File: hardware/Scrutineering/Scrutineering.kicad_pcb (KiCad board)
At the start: 2 copper layers, 52.8 x 51.7 mm, 22 parts, among them J1 Conn_02x04, J10 Conn_01x01, J11 Conn_01x02, J12 Conn_01x02, J2 Conn_02x04, J3 Conn_01x03, J4 Conn_01x03, J5 Conn_01x01, J6 Conn_01x01, J7 Conn_01x01, J8 Conn_01x01, J9 Conn_01x01

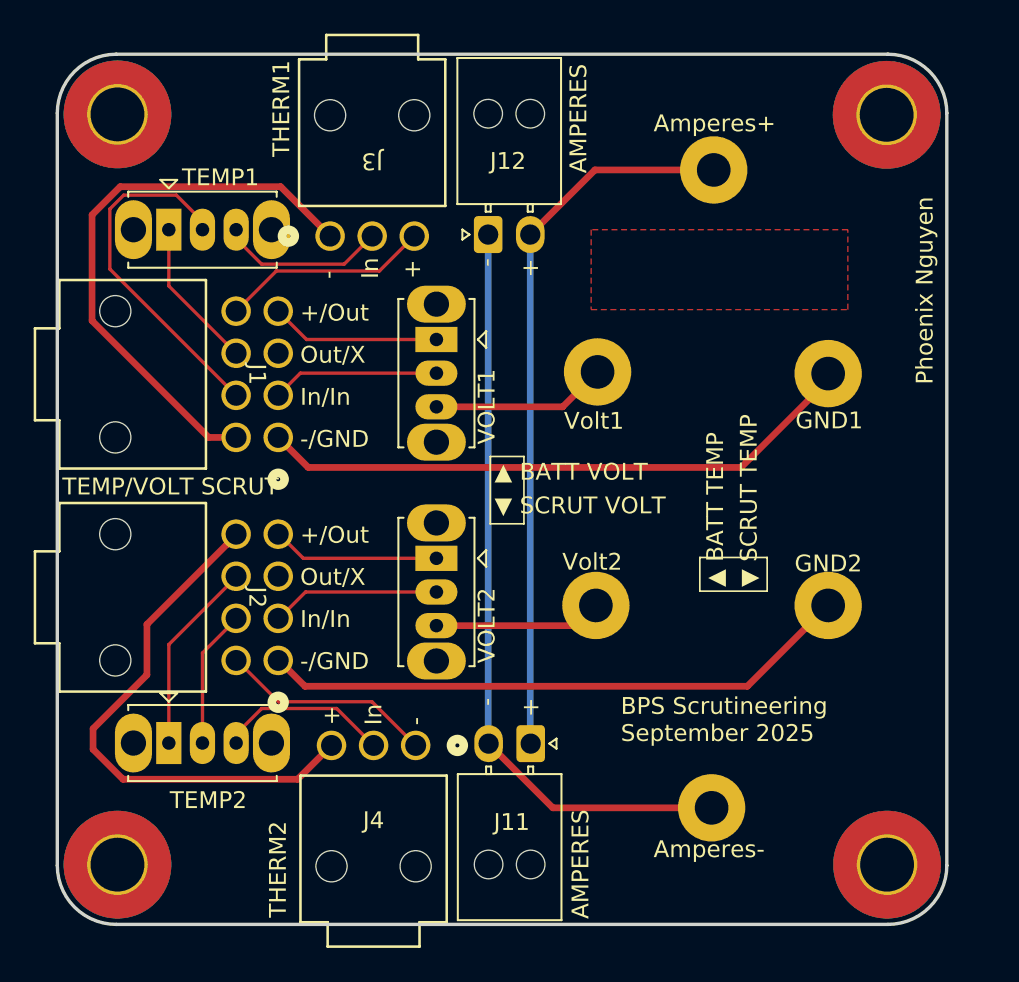
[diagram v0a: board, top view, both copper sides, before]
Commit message: Scrutineering (#7)
* initial schematic and layout

* updated layout

* schematic with graphics/mounting

* graphics stuff

* fixed routing

* BOM and gerber (still need to find jack P/N)

* final

* revert back to main...

* added Scrutineering footprints

* added Scrutineering 3d models

* BOM and gerber with changed connector

* changed to vertical connectors

* added footprints/3d models vertical connectors

* fix 1 trace

* updated BOM

* updated BOM again

* Revert "fix 1 trace"

This reverts commit af0c854c5f9be3b18890f8714f235c97d2fe5d90.

:#

* Replaced Lakshay's tiny banana jacks with real ones

* fix unrouted

* Updated Gerbers

---------

Co-authored-by: Ravi Shah <ravidhruvishshah@gmail.com>
Co-authored-by: kretsdyl <kretschmandk@gmail.com>
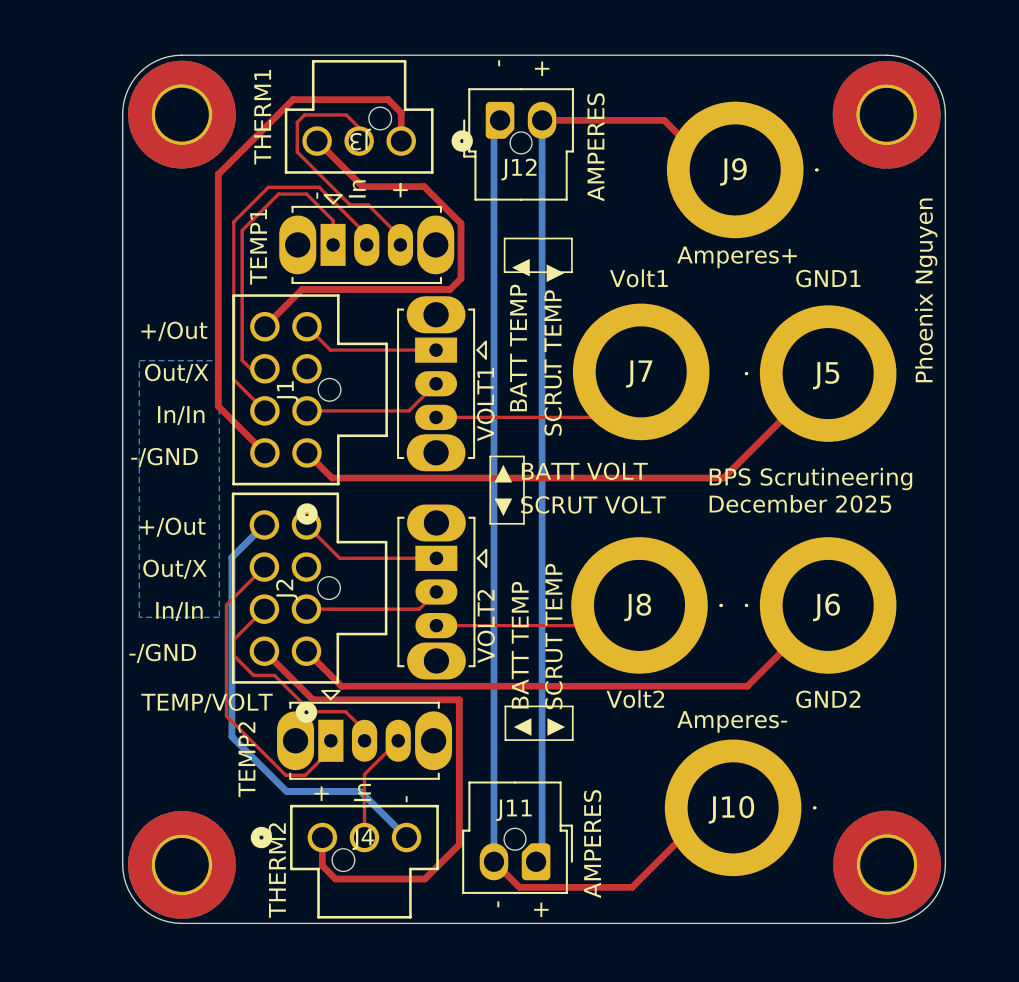
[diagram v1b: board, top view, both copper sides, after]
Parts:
- J1, J2: footprint Scrutineering:nanofit_02x04 -> Scrutineering:CONN_SD-105310-100_08_MOL
- J10, J5, J6, J7, J8, J9: footprint UTSVT_Connectors:Banana_Jack_1_Pin_4mm -> VoltTemp:5754
- J11, J12: footprint UTSVT_Connectors:105313-2102 -> UTSVT_Connectors:Molex_Nano-Fit_105309-xx02_1x02_P2.50mm_Vertical
- J3, J4: footprint VoltTemp:1053131103 -> Scrutineering:CONN_SD-105309-100_03_MOL
- LOGO2: moved to B.Cu
- moved LOGO2 34.6 mm to (94.8, 78.2), turned to 90 degrees
- moved TEMP1 9.80 mm to (103.8, 63.8)
- moved TEMP2 9.63 mm to (103.6, 93.2)
- moved J4 7.79 mm to (103.1, 99.0)
- moved J3 7.05 mm to (107.8, 57.6)
- moved J11 7.03 mm to (115.8, 100.4)
- moved J12 6.82 mm to (113.7, 56.4)
- moved MH3 3.83 mm to (94.8, 56.0)
- moved MH4 3.83 mm to (94.8, 100.6)
- moved J7 2.59 mm to (122.1, 71.3)
- moved J8 2.59 mm to (122.0, 85.2)
- moved J1 1.94 mm to (102.2, 76.1), turned to 90 degrees
- moved J2 1.77 mm to (102.2, 87.9), turned to 90 degrees
- moved J10 1.28 mm to (127.5, 97.2)
- moved J9 1.28 mm to (127.7, 59.3)
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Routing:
- net /GNDA_8: track 12.8 -> 32.4 mm
- net /scrut-: track 45.1 -> 61.0 mm
- net /VDDA_7: track 12.4 -> 26.8 mm
- net /scrut+: track 42.7 -> 56.9 mm
- net /rawTemp7: track 9.00 -> 17.7 mm
- net /VDDA_8: track 32.9 -> 26.2 mm
- net /rawTemp8: track 12.1 -> 18.6 mm
- net /scrutTemp7: track 9.94 -> 15.4 mm
- net /inputTemp8: track 8.92 -> 13.8 mm
- net /scrutTemp8: track 10.2 -> 6.58 mm
- net /scrutVolt7: track 10.4 -> 13.3 mm
- net /scrutVolt8: track 9.97 -> 12.6 mm
- net /inputVolt8: track 10.0 -> 8.14 mm
- net /voltTap7: track 10.1 -> 8.25 mm
- net /inputVolt7: track 9.95 -> 8.34 mm
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- added copper zone on B.Cu, net (none)
- removed copper zone on F.Cu, net (none)
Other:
- board size 52.8 x 51.7 mm -> 48.9 x 51.6 mm
- board text added: "BATT TEMP ▲"
- board text added: "BPS Scrutineering December 2025"
- board text added: "SCRUT TEMP ▼"
- board text added: "TEMP/VOLT"
- board text removed: "BPS Scrutineering September 2025"
- board text removed: "TEMP/VOLT SCRUT"
